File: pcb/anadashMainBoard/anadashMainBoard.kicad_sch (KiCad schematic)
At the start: 17 parts, among them J1 DisplayConnector, J2 LeftKeyConnector, J3 RightKeyConnector, J4 EncoderConnector

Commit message: Fixing alignment, improvements to pcb such as silkscreen.
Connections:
- net GND: now also U1.1 (GND)
- no-connect marks 22 -> 21
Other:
- note added: "A"
- note added: "B"
- note added: "Switch"
- note added: "Switch1"
- note added: "Switch2"
- note added: "Switch3"
- note added: "Switch4"
- note added: "Switch5"
- note added: "Switch6"
- note added: "Switch7"
- note added: "Switch8"

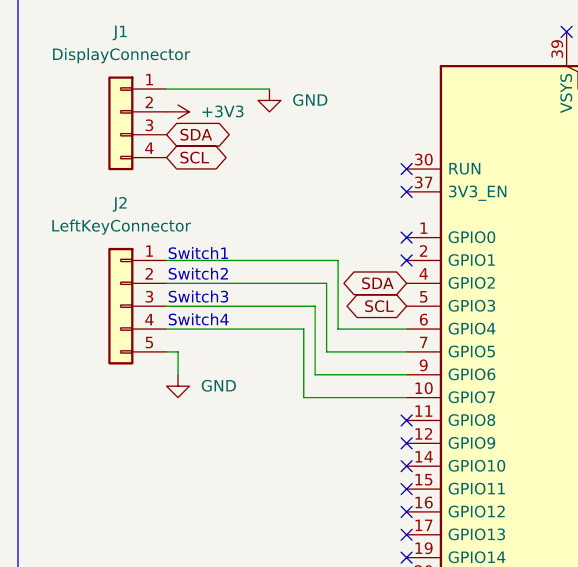
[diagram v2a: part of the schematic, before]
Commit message: Fix wrong pinout order, and wrong GND shape
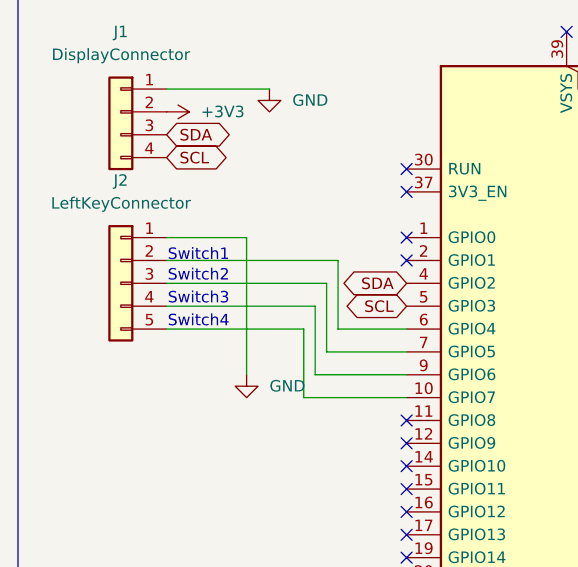
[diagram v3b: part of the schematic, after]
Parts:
- J2: footprint Connector_JST:JST_XH_B5B-XH-A_1x05_P2.50mm_Vertical -> (none)
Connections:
- net GND: now also J2.1 (Pin_1); no longer J2.5 (Pin_5)
- net at A1.10 (GPIO7): now also J2.5 (Pin_5); no longer J2.4 (Pin_4)
- net at A1.6 (GPIO4): now also J2.2 (Pin_2); no longer J2.1 (Pin_1)
- net at A1.7 (GPIO5): now also J2.3 (Pin_3); no longer J2.2 (Pin_2)
- net at A1.9 (GPIO6): now also J2.4 (Pin_4); no longer J2.3 (Pin_3)
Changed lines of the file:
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@@
 	(wire
 		(pts
-			(xy 148.59 88.9) (xy 144.78 88.9)
+			(xy 81.28 78.74) (xy 81.28 93.98)
 		)
 		(stroke
 			(width 0)
 			(type default)
+			(color 0 0 0 1)
 		)
 	)
 	(wire
 		(pts
-			(xy 151.13 101.6) (xy 162.56 101.6)
+			(xy 148.59 88.9) (xy 144.78 88.9)
 		)
 		(stroke
@@
 	(wire
 		(pts
-			(xy 73.66 91.44) (xy 72.39 91.44)
+			(xy 151.13 101.6) (xy 162.56 101.6)
 		)
 		(stroke
 			(width 0)
 			(type default)
-			(color 0 0 0 1)
 		)
 	)
@@
 	(wire
 		(pts
-			(xy 73.66 93.98) (xy 73.66 91.44)
+			(xy 81.28 78.74) (xy 72.39 78.74)
 		)
 		(stroke
@@
 	)
 	(symbol
+		(lib_id "Connector_Generic:Conn_01x05")
+		(at 67.31 83.82 0)
+		(mirror y)
+		(unit 1)
+		(body_style 1)
+		(exclude_from_sim no)
+		(in_bom yes)
+		(on_board yes)
+		(in_pos_files yes)
+		(dnp no)
+		(property "Reference" "J2"
+			(at 67.31 72.39 0)
+			(show_name no)
+			(do_not_autoplace no)
+			(effects
+				(font
+					(size 1.27 1.27)
+				)
+			)
+		)
+		(property "Value" "LeftKeyConnector"
+			(at 67.31 74.93 0)
+			(show_name no)
+			(do_not_autoplace no)
+			(effects
+				(font
+					(size 1.27 1.27)
+				)
+			)
+		)
+		(property "Footprint" ""
+			(at 67.31 83.82 0)
+			(hide yes)
+			(show_name no)
+			(do_not_autoplace no)
+			(effects
+				(font
+					(size 1.27 1.27)
+				)
+			)
+		)
+		(property "Datasheet" ""
+			(at 67.31 83.82 0)
+			(hide yes)
+			(show_name no)
+			(do_not_autoplace no)
+			(effects
+				(font
+					(size 1.27 1.27)
+				)
+			)
+		)
+		(property "Description" "Generic connector, single row, 01x05, script generated (kicad-library-utils/schlib/autogen/connector/)"
+			(at 67.31 83.82 0)
+			(hide yes)
+			(show_name no)
+			(do_not_autoplace no)
+			(effects
+				(font
+					(size 1.27 1.27)
+				)
+			)
+		)
+		(pin "1"
+		)
+		(pin "3"
+		)
+		(pin "4"
+		)
+		(pin "5"
+		)
+		(pin "2"
+		)
+		(instances
+			(project "anadashMainBoard"
+				(path "/be2e610a-0da0-4417-ae24-40d589f4bf40"
+					(reference "J2")
+					(unit 1)
+				)
+			)
+		)
+	)
+	(symbol
 		(lib_id "power:GND")
 		(at 247.65 73.66 0)
@@
 	)
 	(symbol
-		(lib_id "Connector_Generic:Conn_01x05")
-		(at 67.31 86.36 0)
-		(mirror y)
-		(unit 1)
-		(body_style 1)
-		(exclude_from_sim no)
-		(in_bom yes)
-		(on_board yes)
-		(in_pos_files yes)
-		(dnp no)
-		(fields_autoplaced yes)
-		(property "Reference" "J2"
-			(at 67.31 74.93 0)
-			(show_name no)
-			(do_not_autoplace no)
-			(effects
-				(font
-					(size 1.27 1.27)
-				)
-			)
-		)
-		(property "Value" "LeftKeyConnector"
-			(at 67.31 77.47 0)
-			(show_name no)
-			(do_not_autoplace no)
-			(effects
-				(font
-					(size 1.27 1.27)
-				)
-			)
-		)
-		(property "Footprint" "Connector_JST:JST_XH_B5B-XH-A_1x05_P2.50mm_Vertical"
-			(at 67.31 86.36 0)
-			(hide yes)
-			(show_name no)
-			(do_not_autoplace no)
-			(effects
-				(font
-					(size 1.27 1.27)
-				)
-			)
-		)
-		(property "Datasheet" ""
-			(at 67.31 86.36 0)
-			(hide yes)
-			(show_name no)
-			(do_not_autoplace no)
-			(effects
-				(font
-					(size 1.27 1.27)
-				)
-			)
-		)
-		(property "Description" "Generic connector, single row, 01x05, script generated (kicad-library-utils/schlib/autogen/connector/)"
-			(at 67.31 86.36 0)
-			(hide yes)
-			(show_name no)
-			(do_not_autoplace no)
-			(effects
-				(font
-					(size 1.27 1.27)
-				)
-			)
-		)
-		(pin "4"
-		)
-		(pin "5"
-		)
-		(pin "2"
-		)
-		(pin "3"
-		)
-		(pin "1"
-		)
-		(instances
-			(project "anadashMainBoard"
-				(path "/be2e610a-0da0-4417-ae24-40d589f4bf40"
-					(reference "J2")
-					(unit 1)
-				)
-			)
-		)
-	)
-	(symbol
 		(lib_id "power:GND")
 		(at 247.65 93.98 0)
@@
 	(symbol
 		(lib_id "power:GND")
-		(at 73.66 93.98 0)
+		(at 81.28 93.98 0)
 		(unit 1)
 		(body_style 1)
@@
 		(fields_autoplaced yes)
 		(property "Reference" "#PWR02"
-			(at 73.66 100.33 0)
+			(at 81.28 100.33 0)
 			(hide yes)
 			(show_name no)
@@
 		)
 		(property "Value" "GND"
-			(at 76.2 95.2499 0)
+			(at 83.82 95.2499 0)
 			(show_name no)
 			(do_not_autoplace no)
@@
 		)
 		(property "Footprint" ""
-			(at 73.66 93.98 0)
+			(at 81.28 93.98 0)
 			(hide yes)
 			(show_name no)
@@
 		)
 		(property "Datasheet" ""
-			(at 73.66 93.98 0)
+			(at 81.28 93.98 0)
 			(hide yes)
 			(show_name no)
@@
 		)
 		(property "Description" "Power symbol creates a global label with name \"GND\" , ground"
-			(at 73.66 93.98 0)
+			(at 81.28 93.98 0)
 			(hide yes)
 			(show_name no)

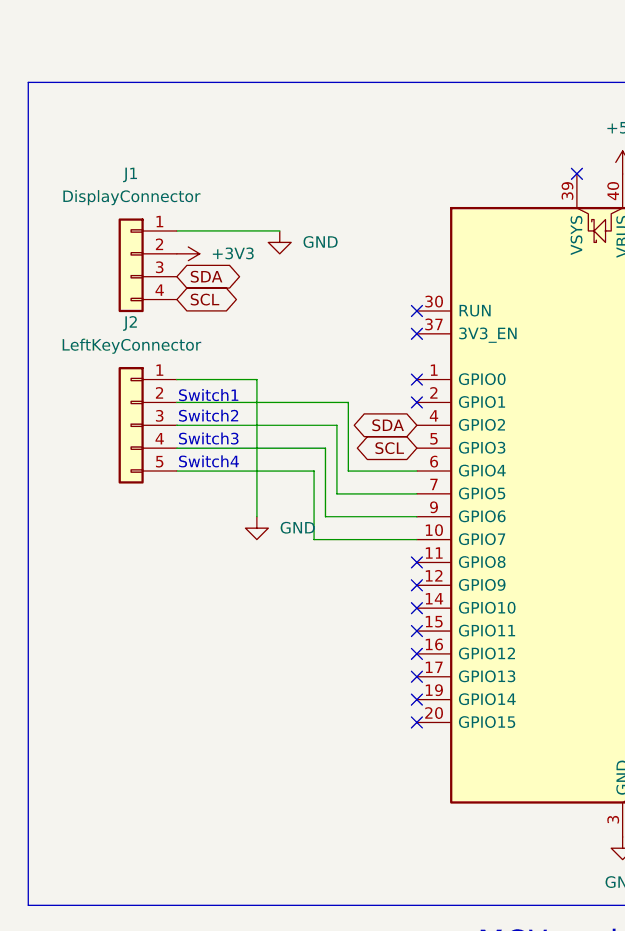
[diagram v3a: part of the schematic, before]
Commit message: Added folk valley cat and hamster to the PCB
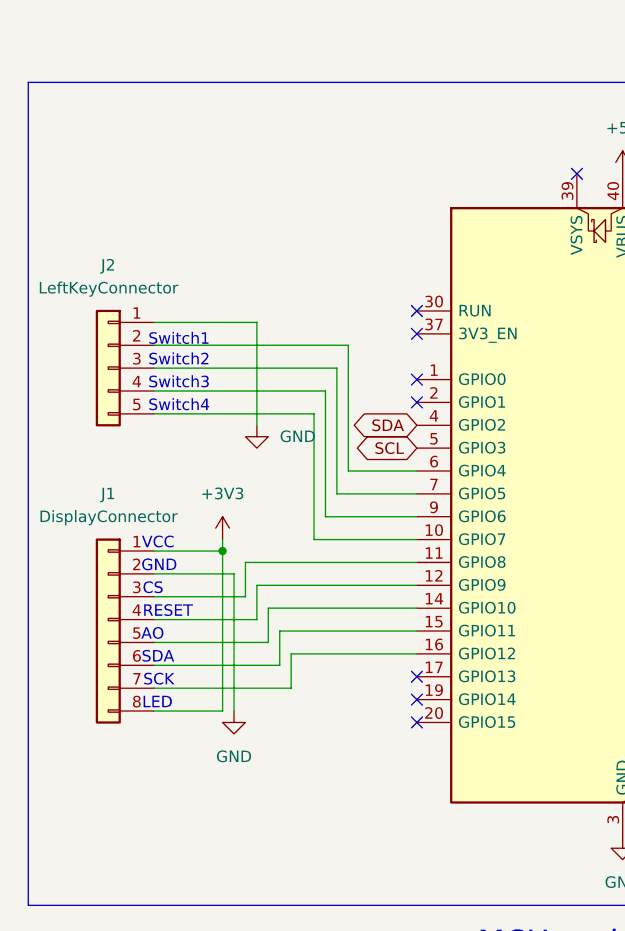
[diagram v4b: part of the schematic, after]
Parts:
- removed J1: DisplayConnector, Connector_JST:JST_XH_B4B-XH-A_1x04_P2.50mm_Vertical, symbol Connector_Generic:Conn_01x04
- added J1: DisplayConnector, Connector_PinHeader_2.54mm:PinHeader_1x08_P2.54mm_Vertical, symbol Connector_Generic:Conn_01x08
- J2: footprint (none) -> Connector_JST:JST_XH_B5B-XH-A_1x05_P2.50mm_Vertical
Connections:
- net +3V3: now also J1.1 (Pin_1), J1.8 (Pin_8)
- net GND: now also J1.2 (Pin_2)
- net at A1.11 (GPIO8): now also J1.3 (Pin_3)
- net at A1.12 (GPIO9): now also J1.4 (Pin_4)
- net at A1.14 (GPIO10): now also J1.5 (Pin_5)
- net at A1.15 (GPIO11): now also J1.6 (Pin_6)
- net at A1.16 (GPIO12): now also J1.7 (Pin_7)
- no-connect marks 21 -> 16
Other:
- note added: "AO"
- note added: "CS"
- note added: "GND"
- note added: "LED"
- note added: "RESET"
- note added: "SCK"
- note added: "SDA"
- note added: "VCC"
- moved on the sheet: J2
